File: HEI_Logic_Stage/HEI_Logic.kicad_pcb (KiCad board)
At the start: 4 copper layers, 61.5 x 67.6 mm, 98 parts, among them J1 RJ_{1}, J2 RJ_{2}, J3 Tag-Connect, J4 Conn_02x10_Odd_Even, J5 430450813_Molex, SW1 SW_SPST, SW2 SW_Push, U1 5V_Converter_R-78E5.0-0.5, U2 ISO6741DWR, U3 B1203XT-1WR3, U4 ADM3058EBRIZ, U5 STM32F334C8T6, U6 LM4132-Q1 SOT-2, U7 ISO7730DWR

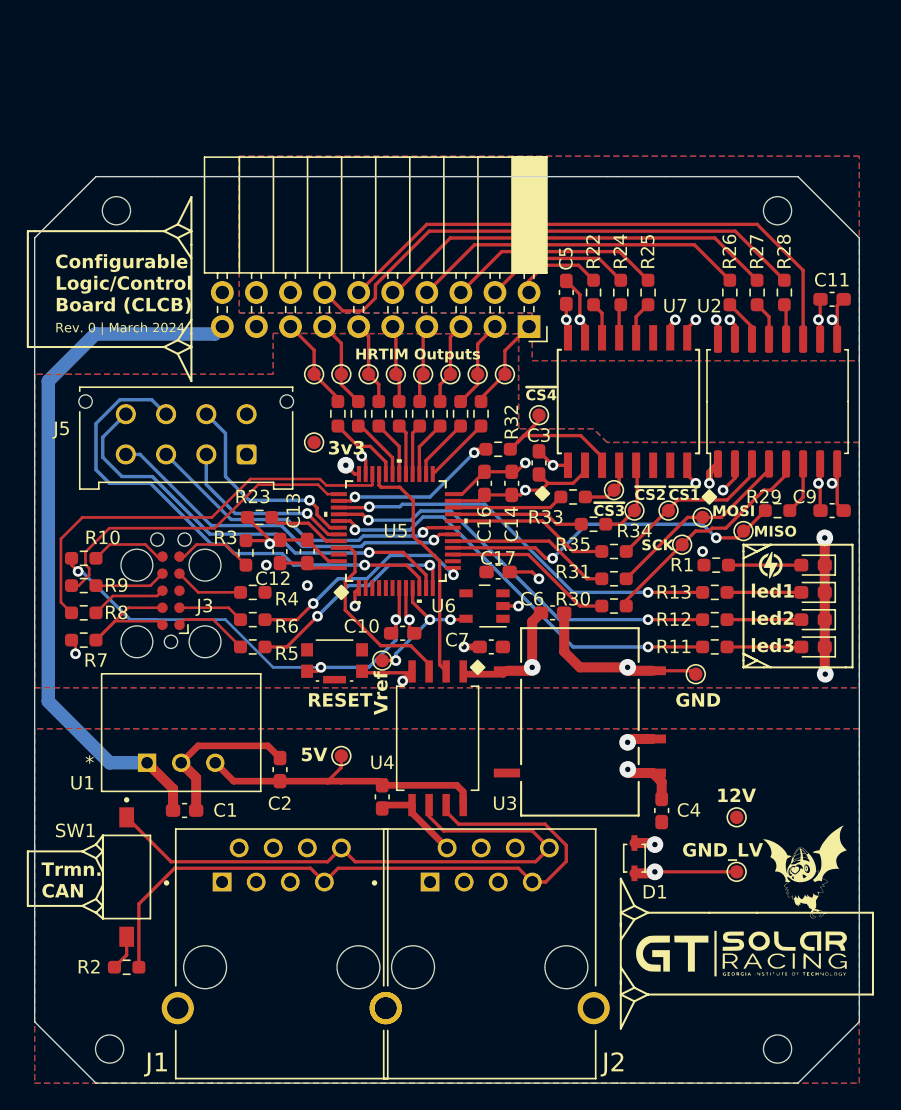
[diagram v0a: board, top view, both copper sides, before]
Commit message: layouted updated HEI-Logic
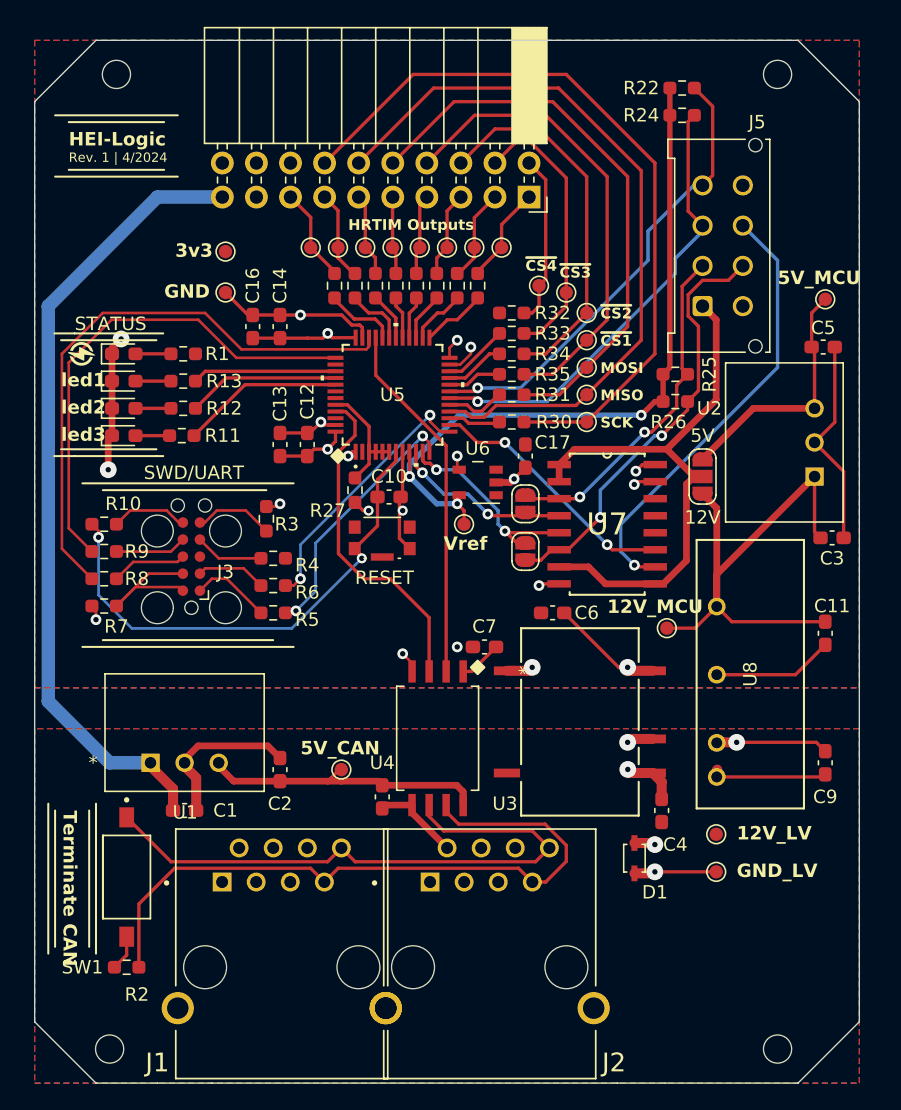
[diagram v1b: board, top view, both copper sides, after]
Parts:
- removed the G*** at (91.9, 137.2)
- removed the G*** at (87.4, 143.3)
- removed the R22 at (76.2, 94.0)
- removed the R22 at (63.2, 103.0)
- removed R23: 10k, Resistor_SMD:R_0603_1608Metric_Pad0.98x0.95mm_HandSolder
- removed R28, R29: 330, Resistor_SMD:R_0603_1608Metric_Pad0.98x0.95mm_HandSolder
- added JP1: Jumper_3_Open, Jumper:SolderJumper-3_P1.3mm_Open_RoundedPad1.0x1.5mm_NumberLabels, F.Cu at (84.3, 107.7)
- added JP4: Jumper_2_Open, Jumper:SolderJumper-2_P1.3mm_Open_RoundedPad1.0x1.5mm, F.Cu at (71.1, 109.7)
- added JP5: Jumper_2_Open, Jumper:SolderJumper-2_P1.3mm_Open_RoundedPad1.0x1.5mm, F.Cu at (71.1, 113.3)
- added R17: 330, Resistor_SMD:R_0603_1608Metric_Pad0.98x0.95mm_HandSolder, F.Cu at (59.9, 93.5)
- added R22: X, Resistor_SMD:R_0603_1608Metric_Pad0.98x0.95mm_HandSolder, F.Cu at (82.8, 78.7)
- added TP22: Test_Point, TestPoint:TestPoint_Pad_D1.0mm, F.Cu at (93.5, 94.5)
- added TP23: Test_Point, TestPoint:TestPoint_Pad_D1.0mm, F.Cu at (81.7, 119.0)
- added U8: TMH 1212S, GTSR_KiCAD_Footprints:TMH SINGLE_TRP, F.Cu at (85.4, 130.1)
- C11, C9: value 0.1uF -> 1uF
- C3, C5: value 0.1uF -> 10uF
- R14, R15, R16, R19, R20, R21: value 47k -> 330
- R24, R25, R26: value 330 -> X
- R27: value 330 -> 10k
- U2: value ISO6741DWR -> 5V_Converter_R-78E5.0-0.5; footprint Package_SO:SOIC-16W_7.5x10.3mm_P1.27mm -> GTSR_KiCAD_Footprints:R-78E5.0-0.5
- U7: value ISO7730DWR -> CD40109BQNSRQ1; footprint GTSR_KiCAD_Footprints:DW0016B_N -> GTSR_KiCAD_Footprints:SOIC127P780X200-16N
- moved D2 53.7 mm to (41.2, 98.6), turned to 0 degrees
- moved D3 53.7 mm to (41.2, 104.6), turned to 0 degrees
- moved D4 53.7 mm to (41.2, 102.6), turned to 0 degrees
- moved D5 53.7 mm to (41.2, 100.6), turned to 0 degrees
- moved G*** 53.7 mm to (38.0, 98.6), turned to 90 degrees
- moved TP12 45.1 mm to (48.8, 94.0)
- moved R11 42.7 mm to (45.5, 104.6), turned to 0 degrees
- moved R1 42.7 mm to (45.6, 98.6), turned to 0 degrees
- moved R12 42.6 mm to (45.6, 102.6), turned to 0 degrees
- moved R13 42.6 mm to (45.6, 100.6), turned to 0 degrees
- moved J5 35.7 mm to (84.3, 95.0), turned to 90 degrees
- moved R27 33.4 mm to (58.4, 108.7)
- moved C11 24.9 mm to (93.5, 119.4), turned to -90 degrees
- moved C3 22.5 mm to (94.0, 112.3), turned to 0 degrees
- moved C16 20.9 mm to (50.8, 96.5), turned to 90 degrees
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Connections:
- C11 pad 1: /SPI_5V -> /12V_MCU
- C11 pad 2: /SPI_GND -> GND
- C3 pad 1: +3V3 -> /12V_MCU
- C5 pad 1: /SPI_5V -> /5V_MCU
- C5 pad 2: /SPI_GND -> GND
- C9 pad 1: +3V3 -> /12V_LV
- C9 pad 2: GND -> /GND_LV
- J4 pad 10: /MOSI_ISO -> /MOSI
- J4 pad 12: /MISO_ISO -> /MISO
- J4 pad 14: /SCK_ISO -> /SCK
- J4 pad 16: /SPI_5V -> GND
- J4 pad 18: /SPI_GND -> +3V3
- J4 pad 2: /~{CS4}_ISO -> /~{CS4}
- J4 pad 4: /~{CS3}_ISO -> /~{CS3}
- J4 pad 6: /~{CS2}_ISO -> /~{CS2}
- J4 pad 8: /~{CS1}_ISO -> /~{CS1}
- J5 pad 1: +3V3 -> /V_Hall
- J5 pad 2: /I2C_SDA -> /HallIN1/TIN3
- J5 pad 3: /AIN4 -> /TIN1
- J5 pad 4: /AIN3 -> /TIN2
- J5 pad 6: /I2C_SCL -> /HallIN2/TIN4
- J5 pad 7: /AIN1 -> /HallIN3
- J5 pad 8: /AIN2 -> GND
- R14 pad 1: /HRTIM_C1 -> /HRTIM_C1_r
- R14 pad 2: /HRTIM_C1_r -> /HRTIM_C1
- R15 pad 1: /HRTIM_C2 -> /HRTIM_C2_r
- R15 pad 2: /HRTIM_C2_r -> /HRTIM_C2
- R16 pad 1: /HRTIM_D1 -> /HRTIM_D1_r
- R16 pad 2: /HRTIM_D1_r -> /HRTIM_D1
- R19 pad 1: /HRTIM_A2 -> /HRTIM_B1
- R19 pad 2: /HRTIM_A2_r -> /HRTIM_B1_r
- R20 pad 1: /HRTIM_B1 -> /HRTIM_B2
- R20 pad 2: /HRTIM_B1_r -> /HRTIM_B2_r
- R21 pad 1: /HRTIM_B2 -> /HRTIM_D2_r
- R21 pad 2: /HRTIM_B2_r -> /HRTIM_D2
- R24 pad 1: Net-(U7-OUTB) -> /Vref
- R24 pad 2: /~{CS3}_ISO -> /TIN1
- R25 pad 1: Net-(U7-OUTC) -> /Vref
- R25 pad 2: /~{CS2}_ISO -> /HallIN1/TIN3
- R26 pad 1: Net-(U2-OUTA) -> /Vref
- R26 pad 2: /~{CS1}_ISO -> /HallIN2/TIN4
- R27 pad 1: Net-(U2-OUTB) -> GND
- R27 pad 2: /MOSI_ISO -> /10kSaver
- U2 pad 1: +3V3 -> /12V_MCU
- U2 pad 3: /~{CS1} -> /5V_MCU
- U5 pad 10: /AIN1 -> /HallIN1_3v3/ADC
- U5 pad 11: /AIN2 -> /HallIN2_3v3/ADC
- U5 pad 14: unconnected-(U5-PA4-Pad14) -> /HallIN3_3v3
- U5 pad 18: /AIN3 -> /TIN1
- U5 pad 19: /AIN4 -> /TIN2
- U5 pad 3: unconnected-(U5-PC14-OSC32_IN-Pad3) -> /10kSaver
- U5 pad 4: unconnected-(U5-PC15-OSC32_OUT-Pad4) -> /10kSaver
- U5 pad 42: /I2C_SCL -> unconnected-(U5-PB6-Pad42)
- U5 pad 43: /I2C_SDA -> unconnected-(U5-PB7-Pad43)
- U5 pad 44: Net-(U5-PH3-BOOT0) -> /10kSaver
- U5 pad 5: unconnected-(U5-PH0-OSC_IN-Pad5) -> /10kSaver
- U5 pad 6: unconnected-(U5-PH1-OSC_OUT-Pad6) -> /10kSaver
- U7 pad 1: +3V3 -> /V_Hall
- U7 pad 10: /SPI_5V -> /HallIN3
- U7 pad 11: unconnected-(U7-NC-Pad11) -> /HallIN3_3v3
- U7 pad 12: Net-(U7-OUTC) -> unconnected-(U7-NC-Pad12)
- U7 pad 13: Net-(U7-OUTB) -> unconnected-(U7-H-Pad13)
- U7 pad 14: Net-(U7-OUTA) -> unconnected-(U7-D-Pad14)
- U7 pad 15: /SPI_GND -> GND
- U7 pad 16: /SPI_5V -> +3V3
- U7 pad 2: GND -> /V_Hall
- U7 pad 3: /~{CS4} -> /HallIN1/TIN3
- U7 pad 4: /~{CS3} -> /HallIN1_3v3/ADC
- U7 pad 5: /~{CS2} -> /HallIN2_3v3/ADC
- U7 pad 6: unconnected-(U7-NC-Pad6) -> /HallIN2/TIN4
- U7 pad 7: unconnected-(U7-NC-Pad7) -> /V_Hall
- U7 pad 9: /SPI_GND -> /V_Hall
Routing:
- net /Vref: track 10.7 -> 54.0 mm
- net /V_Hall: track 0.00 -> 43.1 mm
- net /MISO_ISO: track 41.8 -> 0.00 mm
- net /SCK_ISO: track 39.4 -> 0.00 mm
- net /12V_MCU: track 0.00 -> 39.2 mm
- net /SCK: track 17.0 -> 56.2 mm
- net /AIN1: track 38.0 -> 0.00 mm, vias 1 -> 0
- net /TIN2: track 0.00 -> 34.6 mm, vias 0 -> 1
- net /TIN1: track 0.00 -> 34.2 mm, vias 0 -> 1
- net /HallIN3: track 0.00 -> 33.2 mm, vias 0 -> 1
- net /AIN2: track 32.7 -> 0.00 mm, vias 1 -> 0
- net /HallIN2/TIN4: track 0.00 -> 32.1 mm, vias 0 -> 2
- net /MOSI_ISO: track 30.1 -> 0.00 mm
- net /MISO: track 25.9 -> 55.4 mm, vias 2 -> 0
- net /MOSI: track 14.4 -> 42.7 mm
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- removed copper zone on B.Cu, net /SPI_5V
- removed copper zone on F.Cu, net /SPI_5V
- removed copper zone on In1.Cu, net /SPI_GND
- removed copper zone on In2.Cu, net /SPI_GND
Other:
- board size 61.5 x 67.6 mm -> 61.5 x 77.7 mm
- board text added: "12V_LV"
- board text added: "12V_MCU"
- board text added: "5V_CAN"
- board text added: "5V_MCU"
- board text added: "HEI-Logic"
- board text added: "Rev. 1 | 4/2024"
- board text added: "STATUS"
- board text added: "SWD/UART"
- board text added: "Terminate CAN"
- board text removed: "12V"
- board text removed: "5V"
- board text removed: "Configurable Logic/Control Board (CLCB)"
- board text removed: "Rev. 0 | March 2024"
- board text removed: "Trmn. CAN"

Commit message: initial edits to logic stage schematic
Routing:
- net /CAN_RX: track 24.9 -> 26.3 mm
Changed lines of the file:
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@@
   (segment (start 58.175811 96.403501) (end 57.42981 95.6575) (width 0.25) (layer "F.Cu") (net 5))
   (segment (start 62.501998 113.068001) (end 61.732498 112.298501) (width 0.25) (layer "F.Cu") (net 5))
-  (segment (start 62.6745 121.6025) (end 61.976 120.904) (width 0.2) (layer "F.Cu") (net 5))
   (segment (start 50.8 95.6575) (end 50.4455 95.6575) (width 0.25) (layer "F.Cu") (net 5))
   (segment (start 72.263 115.697) (end 72.136 115.824) (width 0.25) (layer "F.Cu") (net 5))
@@
   (segment (start 54.864 104.447) (end 55.065 104.447) (width 0.25) (layer "F.Cu") (net 5))
   (segment (start 78.994 122.174) (end 78.74 121.92) (width 0.75) (layer "F.Cu") (net 5))
+  (segment (start 62.6745 121.611098) (end 61.971701 120.908299) (width 0.2) (layer "F.Cu") (net 5))
   (segment (start 55.065 104.447) (end 55.88 103.632) (width 0.25) (layer "F.Cu") (net 5))
   (segment (start 94.8425 107.324568) (end 92.673932 105.156) (width 0.25) (layer "F.Cu") (net 5))
@@
   (segment (start 58.967999 97.350001) (end 58.967999 96.5967) (width 0.25) (layer "F.Cu") (net 5))
   (segment (start 65.467999 99.349999) (end 66.264899 99.349999) (width 0.2) (layer "F.Cu") (net 5))
-  (segment (start 62.6745 122.2227) (end 62.6745 121.6025) (width 0.2) (layer "F.Cu") (net 5))
   (segment (start 56.098001 103.850001) (end 56.968001 103.850001) (width 0.25) (layer "F.Cu") (net 5))
   (segment (start 40.3105 98.121118) (end 40.987618 97.444) (width 0.5) (layer "F.Cu") (net 5))
@@
   (segment (start 70.016502 108.137998) (end 70.28125 107.87325) (width 0.5) (layer "F.Cu") (net 5))
   (segment (start 85.3855 122.467401) (end 91.247099 122.467401) (width 0.25) (layer "F.Cu") (net 5))
+  (segment (start 62.6745 122.2227) (end 62.6745 121.611098) (width 0.2) (layer "F.Cu") (net 5))
   (segment (start 40.3105 102.616) (end 40.3105 100.584) (width 0.5) (layer "F.Cu") (net 5))
   (segment (start 57.42981 95.6575) (end 54.356 95.6575) (width 0.25) (layer "F.Cu") (net 5))
@@
   (via (at 67.056 98.044) (size 0.8) (drill 0.4) (layers "F.Cu" "B.Cu") (free) (net 5))
   (via (at 66.04 120.396) (size 0.8) (drill 0.4) (layers "F.Cu" "B.Cu") (free) (net 5))
-  (via (at 61.976 120.904) (size 0.8) (drill 0.4) (layers "F.Cu" "B.Cu") (free) (net 5))
+  (via (at 61.971701 120.908299) (size 0.8) (drill 0.4) (layers "F.Cu" "B.Cu") (free) (net 5))
   (via (at 52.832 109.728) (size 0.8) (drill 0.4) (layers "F.Cu" "B.Cu") (free) (net 5))
   (via (at 40.987618 97.444) (size 1.25) (drill 0.4) (layers "F.Cu" "B.Cu") (free) (net 5))
@@
   (segment (start 59.968 100.153637) (end 59.968 97.350001) (width 0.25) (layer "F.Cu") (net 50))
   (segment (start 65.2145 105.400137) (end 59.968 100.153637) (width 0.25) (layer "F.Cu") (net 50))
-  (segment (start 61.052 115.316) (end 59.060201 115.316) (width 0.25) (layer "F.Cu") (net 51))
-  (segment (start 59.060201 115.316) (end 57.1875 113.443299) (width 0.25) (layer "F.Cu") (net 51))
+  (segment (start 58.236201 114.492) (end 57.1875 113.443299) (width 0.25) (layer "F.Cu") (net 51))
+  (segment (start 57.721302 102.85) (end 56.968001 102.85) (width 0.25) (layer "F.Cu") (net 51))
+  (segment (start 58.42 104.639402) (end 58.42 103.548698) (width 0.25) (layer "F.Cu") (net 51))
+  (segment (start 62.676 114.492) (end 58.236201 114.492) (width 0.25) (layer "F.Cu") (net 51))
+  (segment (start 58.42 103.548698) (end 57.721302 102.85) (width 0.25) (layer "F.Cu") (net 51))
+  (segment (start 63.9445 122.2227) (end 63.9445 115.7605) (width 0.25) (layer "F.Cu") (net 51))
+  (segment (start 63.9445 115.7605) (end 62.676 114.492) (width 0.25) (layer "F.Cu") (net 51))
+  (segment (start 57.1875 105.871902) (end 58.42 104.639402) (width 0.25) (layer "F.Cu") (net 51))
   (segment (start 57.1875 113.443299) (end 57.1875 105.871902) (width 0.25) (layer "F.Cu") (net 51))
-  (segment (start 63.9445 122.2227) (end 63.9445 118.2085) (width 0.25) (layer "F.Cu") (net 51))
-  (segment (start 57.721302 102.85) (end 56.968001 102.85) (width 0.25) (layer "F.Cu") (net 51))
-  (segment (start 57.1875 105.871902) (end 58.42 104.639402) (width 0.25) (layer "F.Cu") (net 51))
-  (segment (start 58.42 103.548698) (end 57.721302 102.85) (width 0.25) (layer "F.Cu") (net 51))
-  (segment (start 63.9445 118.2085) (end 61.052 115.316) (width 0.25) (layer "F.Cu") (net 51))
-  (segment (start 58.42 104.639402) (end 58.42 103.548698) (width 0.25) (layer "F.Cu") (net 51))
   (segment (start 81.3835 102.108) (end 81.3835 100.076) (width 0.4) (layer "F.Cu") (net 52))
   (segment (start 62.484 107.696) (end 62.484 105.865999) (width 0.25) (layer "F.Cu") (net 52))
